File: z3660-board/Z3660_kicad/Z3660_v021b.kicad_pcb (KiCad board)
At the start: 4 copper layers, 173.9 x 92.8 mm, 178 parts, among them CN1 KEL-8817-200-170S-F, CN2 Conn_02x40_Odd_Even, CN3 Conn_02x40_Odd_Even, J1 Jumper_2_Open, J2 Conn_02x07_Odd_Even, U1 LTC2990, U10 74FCT543A, U11 74FCT543A, U12 74FCT543A, U13 74FCT543A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

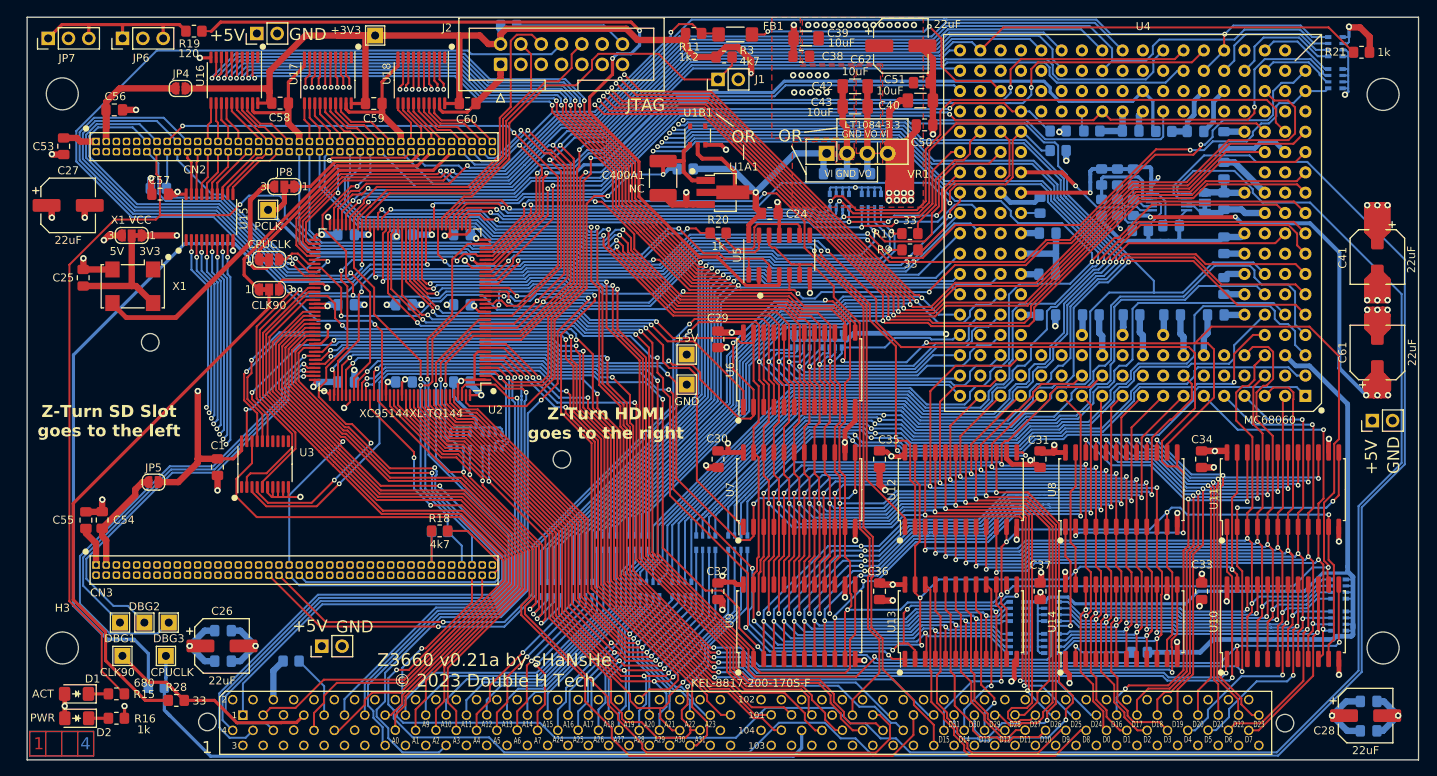
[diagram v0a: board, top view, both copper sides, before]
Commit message: [PCB] v0.21b Update 060 socket
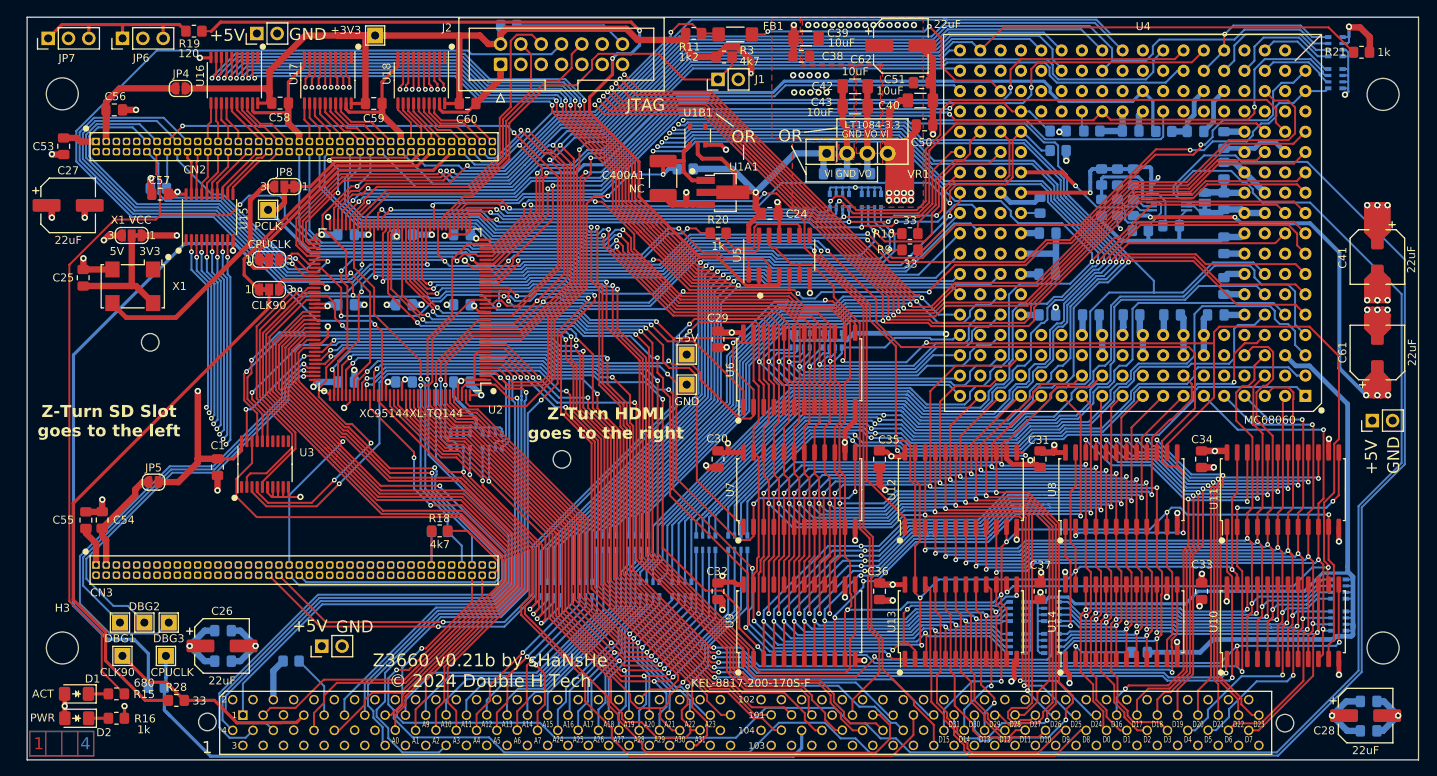
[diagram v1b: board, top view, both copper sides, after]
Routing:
- net 060A28: track 191.4 -> 192.6 mm
- net LEBUS_DMA: track 216.0 -> 214.9 mm
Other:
- board text added: "Z3660 v0.21b by sHaNsHe © 2024 Double H Tech"
- board text removed: "Z3660 v0.21a by sHaNsHe © 2023 Double H Tech"
